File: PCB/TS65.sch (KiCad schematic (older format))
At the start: 219 parts

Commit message: Updating schematic to use STM32F303CC microcontroller instead of ATMEGA32U4; next steps: swapping out USB3 interconnect for HDMI.
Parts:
- BREAKHOLES1, BREAKHOLES2, BREAKHOLES3, BREAKHOLES4, BREAKHOLES5, BREAKHOLES6, FID1, FID2, FID3, FID4, FID5, FID6, FID7, FID8, HOLE1, HOLE2, LOGO1, LOGO2, LOGO3, LOGO4, LOGO5, LOGO6, LOGO7, LOGO8, STAB1, STAB10, STAB11, STAB12, STAB2, STAB3, STAB4, STAB5, STAB6, STAB7, STAB8, STAB9: symbol MISC -> TS65-rescue:MISC
- D1:1, D1:10, D1:11, D1:12, D1:13, D1:14, D1:15, D1:16, D1:2, D1:3, D1:4, D1:5, D1:6, D1:7, D1:8, D1:9, D2:1, D2:10, D2:11, D2:12, D2:13, D2:14, D2:15, D2:16, D2:2, D2:3, D2:4, D2:5, D2:6, D2:8, D2:9, D3:1, D3:10, D3:11, D3:12, D3:13, D3:14, D3:15, D3:16, D3:2, D3:3, D3:4, D3:5, D3:6, D3:8, D3:9, D4:1, D4:10, D4:11, D4:12, D4:13, D4:15, D4:16, D4:2, D4:3, D4:4, D4:5, D4:6, D4:7, D4:8, D4:9, D5:1, D5:10, D5:11, D5:12, D5:13, D5:15, D5:16, D5:2, D5:3, D5:4, D5:5, D5:8: symbol DIODE -> TS65-rescue:DIODE
- S1:1, S1:10, S1:11, S1:12, S1:13, S1:14, S1:15, S1:15_2, S1:16, S1:2, S1:3, S1:4, S1:5, S1:6, S1:7, S1:8, S1:9, S2:1, S2:10, S2:11, S2:12, S2:13, S2:14, S2:15, S2:16, S2:2, S2:3, S2:4, S2:5, S2:6, S2:8, S2:9, S3:1, S3:10, S3:11, S3:12, S3:13, S3:14, S3:15, S3:15_2, S3:15_3, S3:16, S3:1_2, S3:2, S3:3, S3:4, S3:5, S3:6, S3:8, S3:9, S4:1, S4:10, S4:11, S4:12, S4:13, S4:13_2, S4:15, S4:16, S4:1_2, S4:2, S4:3, S4:4, S4:5, S4:6, S4:7, S4:8, S4:9, S5:1, S5:10, S5:10_2, S5:10_3, S5:10_4, S5:10_5, S5:10_6, S5:10_7, S5:11, S5:11_2, S5:11_3, S5:11_4, S5:11_5, S5:12, S5:12_2, S5:12_3, S5:13, S5:13_2, S5:15, S5:15_2, S5:16, S5:1_2, S5:2, S5:2_2, S5:2_3, S5:3, S5:3_2, S5:3_3, S5:3_4, S5:4, S5:4_2, S5:4_3, S5:4_4, S5:4_5, S5:4_6, S5:4_7, S5:5, S5:5_2, S5:5_3, S5:5_4, S5:8, S5:8_2, S5:8_3: symbol SW -> TS65-rescue:SW

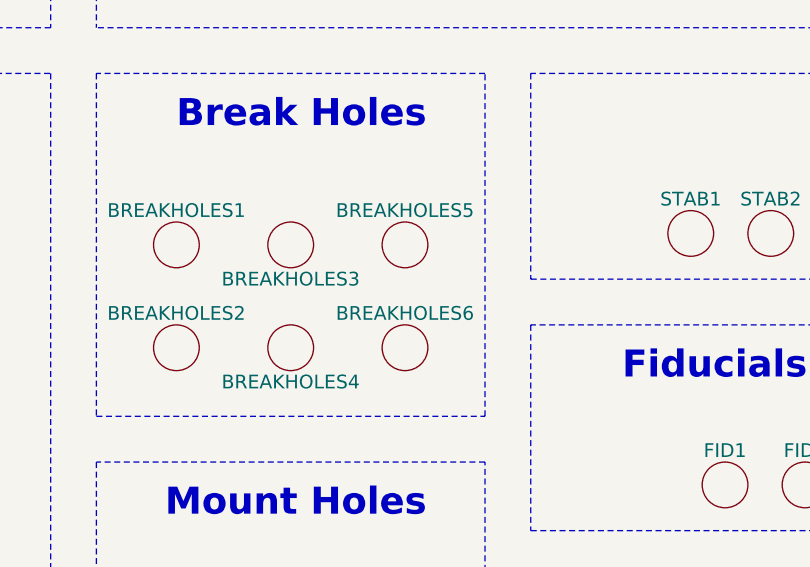
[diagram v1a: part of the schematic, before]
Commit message: Updating design to use STM32F303 instead of AVR32u4.
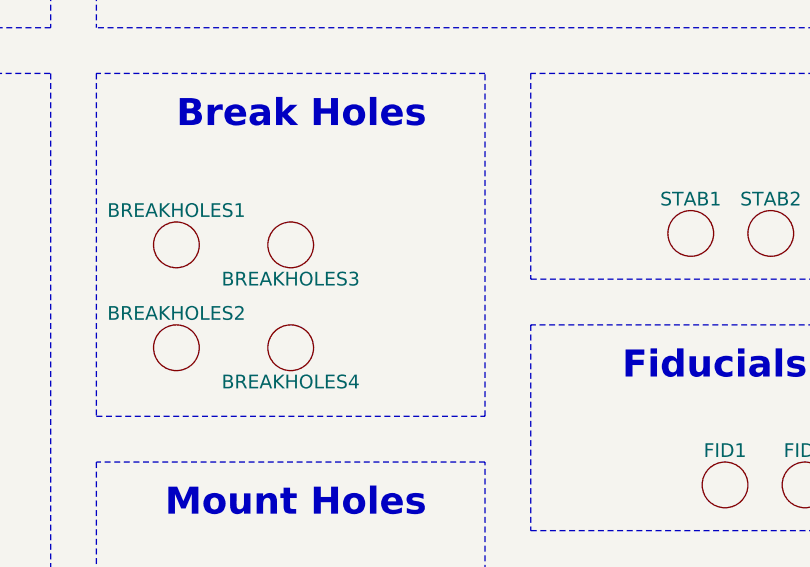
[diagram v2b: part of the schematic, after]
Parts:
- removed BREAKHOLES5, BREAKHOLES6: MISC, prettylib:BreakHoles, symbol TS65-rescue:MISC
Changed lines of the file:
@@
 	5200 7550 4250 7550
-$Comp
-L TS65-rescue:MISC BREAKHOLES6
-U 1 1 573F8792
-P 9500 7800
-F 0 "BREAKHOLES6" H 9500 7950 60  0000 C CNN
-F 1 "MISC" H 9500 7650 60  0001 C CNN
-F 2 "prettylib:BreakHoles" H 9500 7800 60  0001 C CNN
-F 3 "" H 9500 7800 60  0000 C CNN
-	1    9500 7800
-	1    0    0    -1
-$EndComp
-$Comp
-L TS65-rescue:MISC BREAKHOLES5
-U 1 1 573F8798
-P 9500 7350
-F 0 "BREAKHOLES5" H 9500 7500 60  0000 C CNN
-F 1 "MISC" H 9500 7200 60  0001 C CNN
-F 2 "prettylib:BreakHoles" H 9500 7350 60  0001 C CNN
-F 3 "" H 9500 7350 60  0000 C CNN
-	1    9500 7350
-	1    0    0    -1
-$EndComp
 $Comp
 L TS65-rescue:MISC BREAKHOLES4
